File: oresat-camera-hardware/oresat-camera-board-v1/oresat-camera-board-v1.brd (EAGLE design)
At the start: 31.5 x 14 mm, 41 parts, among them J1 4-1734742-0, U1 AR0134CSSM00SPCA0, U2 TPS70618DRVR, U3 TPS71928-28DRVT, U4 TPS71928-28DRVT, X1 KC2520B27.0000C10E00

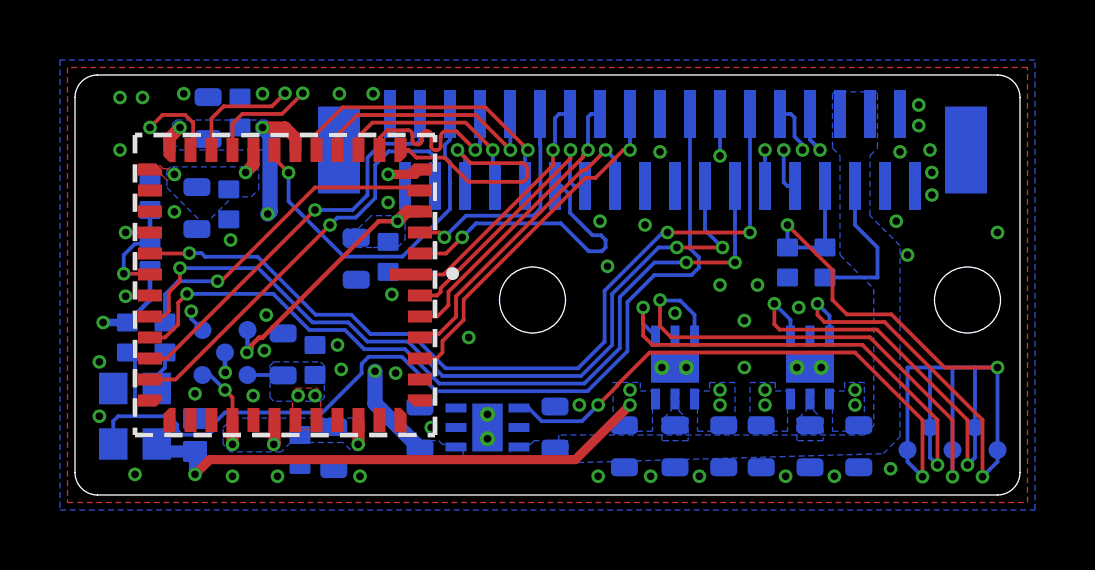
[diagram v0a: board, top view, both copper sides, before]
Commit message: added i2c pullups
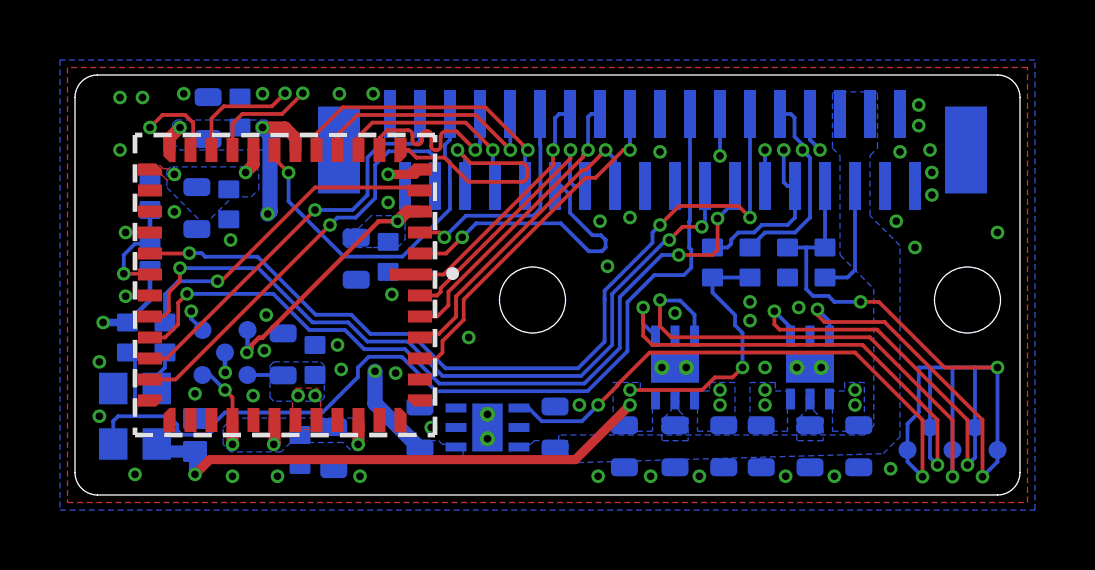
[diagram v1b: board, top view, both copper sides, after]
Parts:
- added R7, R8: 4.7k, oresat-rcl:.0402-B
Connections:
- net N$3: now also R8.1
- net N$4: now also R7.1
- net VDD_IO: now also R7.2, R8.2
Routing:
- net VDD_IO: track 50.0 -> 58.7 mm, vias 8 -> 9
- net N$4: track 22.8 -> 27.6 mm
- net N$3: track 22.8 -> 27.1 mm
- net VREG_EN: track 104.2 -> 101.6 mm
- net N$10: track 26.9 -> 25.6 mm
- net 3.3V: track 5.11 -> 3.90 mm
- net N$8: track 27.0 -> 26.4 mm
- net GND: vias 54 -> 53
